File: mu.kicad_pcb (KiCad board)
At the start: 4 copper layers, 54 x 67.2 mm, 72 parts, among them J1 USB_C_Receptacle_USB2.0_16P, J2 Conn_02x03_Odd_Even, J4 2060-1452/998-404, J5 ESQ-110-X-X-D, U1 STM32F042F6P6, U10 TLV3603QDCKRQ1, U11 SN74LVC1G74DCUT, U12 LM4040AIM3-2.5/NOPB, U13 MCP4921-E/SN, U14 BMP390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

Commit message: progress
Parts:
- moved C17 10.4 mm to (146.5, 113.5), turned to 90 degrees
- moved J5 8.73 mm to (133.0, 78.5)
- moved C10 5.07 mm to (171.0, 109.0)
- moved C4 5.07 mm to (174.0, 109.0)
- moved C7 5.07 mm to (178.5, 116.5)
- moved D1 5.07 mm to (173.5, 112.0)
- moved L1 5.07 mm to (175.5, 116.0)
- moved R1 5.07 mm to (175.5, 108.5)
- moved R2 5.07 mm to (177.5, 108.5)
- moved R4 5.07 mm to (172.5, 109.5)
- moved U2 5.07 mm to (176.5, 111.5)
- moved C12 1.76 mm to (148.5, 105.0), turned to 90 degrees
- moved C11 1.69 mm to (149.5, 105.0), turned to 90 degrees
- moved U5 1.00 mm to (152.0, 115.0), turned to 0 degrees
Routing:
- net 5V: track 22.5 -> 91.3 mm, vias 0 -> 4
- net VBAT_Local: track 1.93 -> 62.4 mm, vias 0 -> 2
- net 3.3V_Dig: track 23.3 -> 82.6 mm, vias 1 -> 7
- net HV: track 13.2 -> 44.1 mm
- net SPI_SCK: track 0.00 -> 30.2 mm
- net SPI_MOSI: track 0.00 -> 28.2 mm
- net CAN_hi: track 2.03 -> 28.7 mm
- net CAN_lo: track 3.83 -> 28.5 mm
- net VBUS_RAW: track 16.8 -> 39.4 mm, vias 2 -> 4
- net Latch_Out: track 0.00 -> 21.2 mm, vias 0 -> 2
- net Latch_Rst: track 2.60 -> 22.4 mm, vias 0 -> 2
- net SPI_CS_DAC: track 0.00 -> 17.5 mm
- net SPI_MISO: track 0.00 -> 14.4 mm, vias 0 -> 2
- net SPI_CS_FLASH: track 0.00 -> 13.8 mm, vias 0 -> 2
- net SPI_CS_BMP: track 0.00 -> 8.11 mm, vias 0 -> 2
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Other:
- board size 54 x 67.2 mm -> 55.5 x 67.2 mm

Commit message: progress2
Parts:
- moved J2 1.74 mm to (146.0, 104.0)
- moved C11 1.38 mm to (148.5, 106.0), turned to -90 degrees
- moved C12 1.37 mm to (149.5, 106.0), turned to -90 degrees
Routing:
- net PA12: track 0.00 -> 6.26 mm
- net PA11: track 0.00 -> 4.52 mm
- net GND: track 47.2 -> 48.9 mm, vias 59 -> 60
- net CAN_tx: track 6.01 -> 5.01 mm
- net 3.3V_Dig: track 82.6 -> 83.5 mm
- net CAN_rx: track 5.98 -> 5.26 mm
- net USB_DP: vias 0 -> 1
- net USB_DN: vias 0 -> 1

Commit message: progress3
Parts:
- moved D3 10.4 mm to (133.1, 94.5), turned to 90 degrees
- moved R14 7.42 mm to (133.0, 97.0), turned to 180 degrees
- moved J5 4.55 mm to (129.3, 81.1), turned to -90 degrees
- moved R10 4.48 mm to (136.5, 101.0), turned to 0 degrees
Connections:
- net USB_DN renamed USB_D-
- net USB_DP renamed USB_D+
- D3 pad 1: CAN_hi -> CAN_+
- D3 pad 2: CAN_lo -> CAN_-
- J2 pad 1: CAN_rx -> CAN_rx-
- J2 pad 2: CAN_tx -> CAN_tx+
- J2 pad 3: PA11 -> PA11-
- J2 pad 4: PA12 -> PA12+
- R14 pad 1: CAN_hi -> CAN_+
- R14 pad 2: CAN_lo -> CAN_-
- U9 pad 6: CAN_lo -> CAN_-
- U9 pad 7: CAN_hi -> CAN_+
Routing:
- net CAN_hi: track 28.7 -> 0.00 mm
- net CAN_lo: track 28.5 -> 0.00 mm
- net CAN_-: track 0.00 -> 2.89 mm
- net CAN_+: track 0.00 -> 1.85 mm
- net Net-(U9-Rs): track 1.38 -> 2.80 mm
- net PA11: track 4.52 -> 5.54 mm
- net USB_D+: track 1.02 -> 0.00 mm

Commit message: nearly done now
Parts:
- C10, C4, C7, D1, L1, R1, R2, R4, U2: moved to F.Cu
- G***: moved to B.Cu
- moved G*** 30.9 mm to (130.5, 104.0), turned to -90 degrees
- moved C10 8.45 mm to (179.0, 106.4)
- moved C7 7.45 mm to (171.5, 113.9)
- moved R4 5.70 mm to (177.5, 106.9), turned to 180 degrees
- moved R2 5.64 mm to (172.5, 105.9), turned to 0 degrees
- moved D3 4.20 mm to (130.5, 97.8), turned to -90 degrees
- moved D1 4.02 mm to (176.5, 109.4)
- moved U2 3.97 mm to (173.5, 108.9)
- moved C4 3.33 mm to (176.0, 106.4)
- moved C14 3.12 mm to (149.0, 92.5)
- moved C16 3.12 mm to (149.0, 90.5)
- moved D2 3.12 mm to (147.5, 94.5)
- moved U4 3.12 mm to (151.9, 92.1)
- moved R14 3.10 mm to (130.5, 95.2), turned to 0 degrees
- moved L1 2.81 mm to (174.5, 113.4), turned to 0 degrees
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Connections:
- D3 pad 1: CAN_+ -> CAN_o+
- D3 pad 2: CAN_- -> CAN_o-
- J2 pad 1: CAN_rx- -> CAN_-
- J2 pad 2: CAN_tx+ -> CAN_+
- J2 pad 3: PA11- -> PA-
- J2 pad 4: PA12+ -> PA+
- J5 pad 15: CAN_lo -> CAN_o-
- J5 pad 16: CAN_hi -> CAN_o+
- R14 pad 1: CAN_+ -> CAN_o+
- R14 pad 2: CAN_- -> CAN_o-
- U1 pad 17: PA11 -> PA-
- U1 pad 18: PA12 -> PA+
- U3 pad 1: GND -> Net-(U6-NONIINVERTINGINPUT)
- U3 pad 2: Net-(U6-NONIINVERTINGINPUT) -> unconnected-(U3-Pad2)
- U9 pad 1: CAN_tx -> CAN_+
- U9 pad 4: CAN_rx -> CAN_-
- U9 pad 6: CAN_- -> CAN_o-
- U9 pad 7: CAN_+ -> CAN_o+
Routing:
- net 3.3V_Dig: track 83.5 -> 118.3 mm, vias 7 -> 10
- net USB_D-: track 0.00 -> 25.3 mm
- net USB_D+: track 0.00 -> 20.6 mm
- net CAN_o+: track 0.00 -> 14.8 mm
- net CAN_o-: track 0.00 -> 14.3 mm
- net 5V: track 91.3 -> 80.2 mm
- net HV: track 44.1 -> 54.8 mm, vias 1 -> 0
- net SPI_SCK: track 30.2 -> 38.5 mm, vias 0 -> 2
- net VBUS_RAW: track 39.4 -> 47.0 mm
- net CAN_+: track 1.85 -> 9.02 mm
- net PA+: track 0.00 -> 7.11 mm
- net Net-(J1-D+-PadA6): track 6.92 -> 0.07 mm
- net CAN_-: track 2.89 -> 9.35 mm
- net PA12: track 6.26 -> 0.00 mm
- net PA11: track 5.54 -> 0.00 mm
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- removed copper zone on B.Cu, net GND
- removed copper zone on F.Cu, net GND
- removed copper zone on In1.Cu, net GND
- removed copper zone on In2.Cu, net GND
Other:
- board text added: "*"
- board text added: "+"
- board text added: "-"
- board text removed: "SCL SDA +,- OUT RST"

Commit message: restructuring now that we've got the standard connector
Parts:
- added C31: 47uF, Capacitor_SMD:C_0402_1005Metric, B.Cu at (136.1, 127.8)
- added G***: LOGO, LOGO, F.Cu at (147.5, 79.5)
- added R17: 60Ω, Resistor_SMD:R_0402_1005Metric, B.Cu at (135.1, 127.8)
- J4: moved to B.Cu
- R14: value 120Ω -> 60Ω
- moved J4 66.6 mm to (154.4, 50.8)
- moved C29 38.3 mm to (150.0, 62.6), turned to 180 degrees
- moved C28 36.4 mm to (150.1, 63.6), turned to 180 degrees
- moved U8 34.2 mm to (143.9, 68.6), turned to 0 degrees
- moved D3 33.8 mm to (136.1, 131.1)
- moved R14 33.2 mm to (137.1, 127.8), turned to -90 degrees
- moved D2 32.2 mm to (164.4, 67.1), turned to -90 degrees
- moved R11 31.4 mm to (146.6, 68.2), turned to -90 degrees
- moved R10 31.2 mm to (141.9, 131.6)
- moved C12 31.2 mm to (155.6, 135.5)
- moved C13 31.2 mm to (165.2, 133.7)
- moved C8 31.2 mm to (165.2, 136.9)
- moved C9 31.2 mm to (165.2, 137.9)
- moved FB1 31.2 mm to (165.2, 135.9)
- moved R5 31.2 mm to (165.2, 134.7)
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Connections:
- R14 pad 1: CAN_o+ -> Net-(C31-Pad1)
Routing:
- net 3.3V_Dig: track 118.3 -> 40.5 mm, vias 10 -> 11
- net HV: track 54.8 -> 3.57 mm
- net VBUS_RAW: track 47.0 -> 12.5 mm
- net VBAT_Local: track 65.8 -> 32.7 mm
- net 5V: track 80.2 -> 52.7 mm, vias 4 -> 3
- net USB_D-: track 25.3 -> 0.00 mm, vias 1 -> 2
- net USB_D+: track 20.6 -> 0.00 mm, vias 1 -> 0
- net Latch_Rst: track 22.2 -> 4.03 mm, vias 2 -> 3
- net Latch_Out: track 20.6 -> 2.51 mm, vias 2 -> 4
- net SPI_SCK: track 38.5 -> 22.5 mm
- net CAN_o+: track 14.8 -> 0.03 mm
- net CAN_o-: track 14.3 -> 0.00 mm
- net SPI_MOSI: track 26.6 -> 16.2 mm
- net SPI_CS_FLASH: track 13.8 -> 3.59 mm
- net SPI_CS_DAC: track 16.9 -> 8.58 mm
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- added copper zone on B.Cu, net GND
- added copper zone on F.Cu, net GND
- added copper zone on In1.Cu, net GND
- added copper zone on In2.Cu, net GND
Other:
- board size 55.5 x 67.2 mm -> 60 x 60 mm

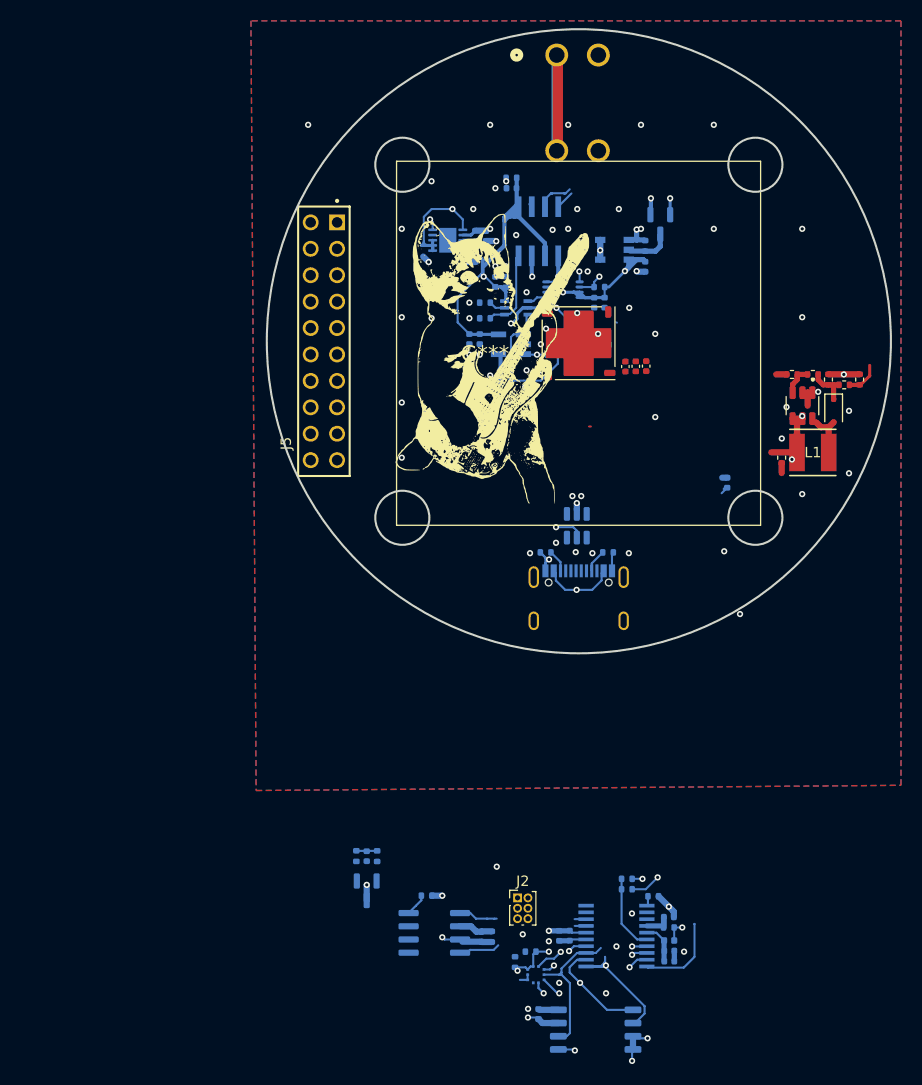
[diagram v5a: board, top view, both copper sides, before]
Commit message: restructuring now that we've got the standard connector part 2
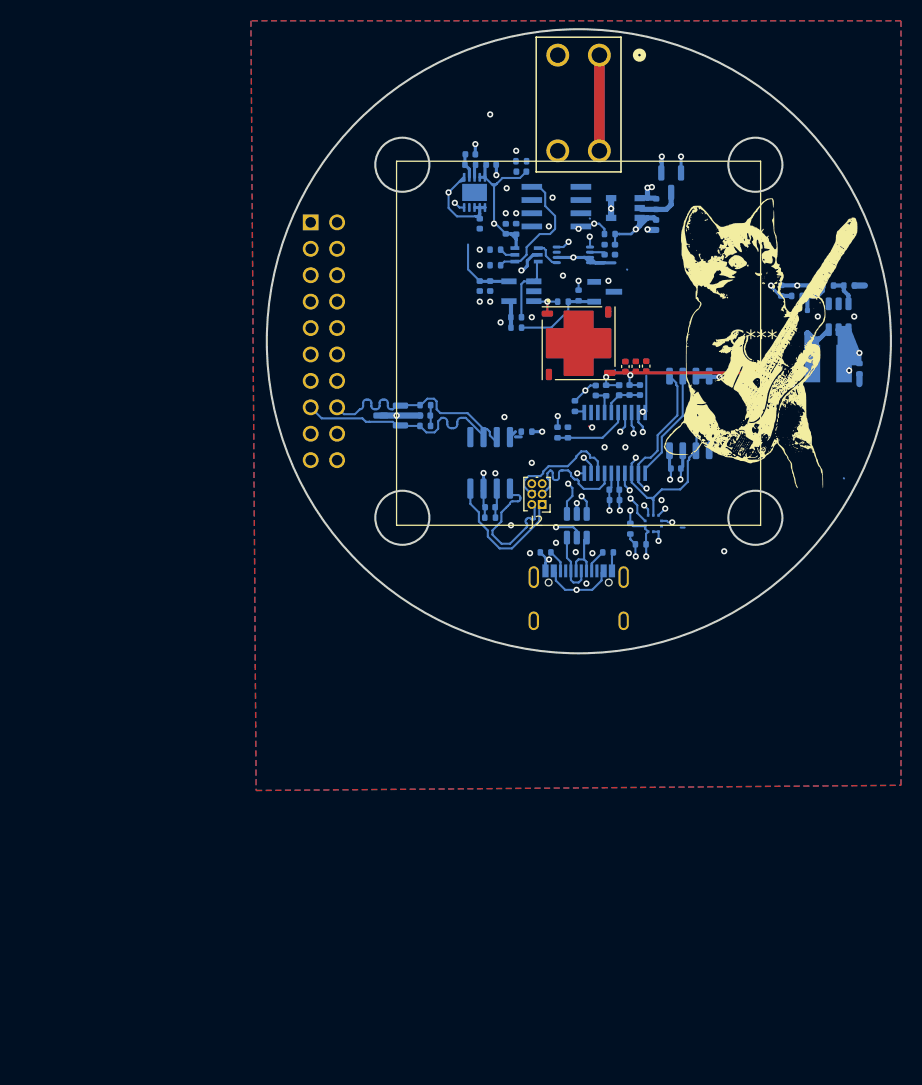
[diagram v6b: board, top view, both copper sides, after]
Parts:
- C10, C4, C7, D1, J5, L1, R1, R2, R4, U2: moved to B.Cu
- J4: moved to F.Cu
- moved U5 59.9 mm to (167.1, 85.2), turned to 90 degrees
- moved C9 55.0 mm to (162.4, 83.0), turned to 90 degrees
- moved C17 54.1 mm to (165.9, 90.5), turned to 180 degrees
- moved C8 54.1 mm to (161.4, 83.0), turned to 90 degrees
- moved FB1 53.1 mm to (160.4, 83.0), turned to -90 degrees
- moved R5 52.0 mm to (159.1, 83.0), turned to 90 degrees
- moved C13 51.1 mm to (158.1, 83.0), turned to 90 degrees
- moved R6 47.7 mm to (156.1, 84.5), turned to 90 degrees
- moved U1 47.4 mm to (160.0, 88.1), turned to -90 degrees
- moved D3 45.7 mm to (138.4, 85.5), turned to 180 degrees
- moved R10 45.6 mm to (151.5, 87.0)
- moved U9 45.5 mm to (148.0, 90.0), turned to 90 degrees
- moved U14 44.8 mm to (163.7, 95.8), turned to 0 degrees
- moved R13 44.3 mm to (155.5, 87.1), turned to -90 degrees
- moved R17 43.9 mm to (141.8, 84.5), turned to 0 degrees
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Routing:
- net 5V: track 52.7 -> 30.4 mm
- net CAN_o-: track 0.00 -> 20.9 mm
- net CAN_o+: track 0.03 -> 20.9 mm
- net HV: track 3.57 -> 16.7 mm, vias 0 -> 1
- net PA+: track 1.10 -> 12.3 mm
- net Net-(D1-A): track 3.56 -> 14.5 mm
- net PA-: track 1.10 -> 11.8 mm
- net CAN_+: track 3.75 -> 14.2 mm
- net CAN_-: track 3.97 -> 14.2 mm
- net SPI_SCK: track 22.5 -> 13.8 mm, vias 2 -> 1
- net USB_D+: track 0.00 -> 7.81 mm, vias 0 -> 1
- net USB_D-: track 0.00 -> 7.53 mm, vias 2 -> 1
- net Net-(J1-D+-PadA6): track 0.07 -> 6.38 mm
- net Net-(J1-D--PadA7): track 0.36 -> 5.43 mm
- net SPI_CS_DAC: track 8.58 -> 3.60 mm
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
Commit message: routed
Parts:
- moved R10 0.71 mm to (152.0, 87.5)
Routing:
- net 3.3V_Dig: track 38.4 -> 130.1 mm
- net 5V: track 30.4 -> 89.0 mm, vias 3 -> 4
- net VBUS_RAW: track 12.6 -> 60.1 mm
- net SPI_SCK: track 13.8 -> 51.9 mm, vias 1 -> 3
- net SPI_MOSI: track 16.5 -> 43.5 mm, vias 2 -> 3
- net SPI_CS_DAC: track 3.60 -> 27.8 mm, vias 0 -> 2
- net VBAT_Local: track 30.5 -> 53.7 mm
- net Latch_Rst: track 5.13 -> 26.2 mm, vias 3 -> 2
- net Latch_Out: track 3.10 -> 23.2 mm
- net SPI_CS_BMP: track 2.91 -> 16.2 mm
- net SPI_MISO: track 14.3 -> 21.5 mm
- net SPI_CS_FLASH: track 3.98 -> 10.7 mm
- net GND: track 48.7 -> 49.6 mm, vias 56 -> 54

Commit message: route2
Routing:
- net HV: track 16.6 -> 23.5 mm
- net Net-(R11-Pad2): track 1.25 -> 2.70 mm
- net 5V: track 89.0 -> 90.0 mm
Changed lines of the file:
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@@
 	)
 	(segment
-		(start 173.17 81.35)
-		(end 173.5 81.02)
+		(start 159.5 81.35)
+		(end 173.17 81.35)
 		(width 0.3)
 		(layer "F.Cu")
@@
 	)
 	(segment
-		(start 159.5 81.35)
-		(end 173.17 81.35)
-		(width 0.3)
+		(start 159.371899 81.478101)
+		(end 159.5 81.35)
+		(width 0.2)
 		(layer "F.Cu")
 		(net 4)
 	)
 	(segment
-		(start 159.371899 81.478101)
-		(end 159.5 81.35)
-		(width 0.2)
+		(start 175.5 79.02)
+		(end 175.5 75)
+		(width 0.3)
 		(layer "F.Cu")
 		(net 4)
 	)
-	(via
-		(at 175 72.952)
-		(size 0.6)
-		(drill 0.3)
-		(layers "F.Cu" "B.Cu")
+	(segment
+		(start 173.17 81.35)
+		(end 175.5 79.02)
+		(width 0.3)
+		(layer "F.Cu")
 		(net 4)
 	)
+	(via
+		(at 175.5 75)
+		(size 0.6)
+		(drill 0.3)
+		(layers "F.Cu" "B.Cu")
+		(net 4)
+	)
+	(segment
+		(start 175.5 74.3515)
+		(end 175.5 75)
+		(width 0.3)
+		(layer "B.Cu")
+		(net 4)
+	)
 	(segment
 		(start 175.8995 73.952)
-		(end 175.034 73.0865)
+		(end 175.5 74.3515)
 		(width 0.3)
 		(layer "B.Cu")
@@
 	)
 	(segment
+		(start 151.5 61)
+		(end 151.5 61.98)
+		(width 0.2)
+		(layer "B.Cu")
+		(net 9)
+	)
+	(segment
 		(start 150.5 68.48)
 		(end 150 67.98)
@@
 		(start 148.371899 63.421899)
 		(end 148.371899 67)
+		(width 0.2)
+		(layer "B.Cu")
+		(net 9)
+	)
+	(segment
+		(start 151.5 61.98)
+		(end 151.48 62)
 		(width 0.2)
 		(layer "B.Cu")
@@
 	(segment
 		(start 146.5 62.55)
+		(end 146.5 64)
+		(width 0.2)
+		(layer "B.Cu")
+		(net 42)
+	)
+	(segment
+		(start 146.5 61.431)
+		(end 146.5 62.55)
+		(width 0.2)
+		(layer "B.Cu")
+		(net 42)
+	)
+	(segment
+		(start 146.595 61.336)
 		(end 146.5 61.431)
-		(width 0.3)
-		(layer "B.Cu")
-		(net 42)
-	)
-	(segment
-		(start 146.5 61.431)
-		(end 146.595 61.336)
-		(width 0.2)
-		(layer "B.Cu")
+		(width 0.2)
+		(layer "B.Cu")
